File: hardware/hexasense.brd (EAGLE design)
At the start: 100 x 62 mm, 41 parts

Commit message: added GND around PWM lines leading to LEDs
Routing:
- net N$4: track 91.8 -> 100.8 mm
- net N$19: track 75.8 -> 83.9 mm, vias 1 -> 0
- net N$7: track 78.1 -> 84.7 mm
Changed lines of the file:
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@@
 <via x="89.46" y="24.19" extent="1-16" drill="0.3"/>
 <via x="70.96" y="2.73" extent="1-16" drill="0.3"/>
+<polygon width="0.254" layer="1" isolate="0.254" orphans="yes">
+<vertex x="65.77" y="31.02"/>
+<vertex x="65.77" y="47.78"/>
+<vertex x="57.36" y="56.19"/>
+<vertex x="17.49" y="56.19"/>
+<vertex x="17.49" y="52.95"/>
+<vertex x="17.49" y="51.49"/>
+<vertex x="40.61" y="51.49"/>
+<vertex x="56.26" y="51.49"/>
+<vertex x="61.43" y="46.32"/>
+<vertex x="61.43" y="31.02"/>
+</polygon>
 <wire x1="41.11" y1="43.83" x2="41.085" y2="46.89" width="0" layer="19" extent="16-16"/>
 </signal>
@@
 <contactref element="LED4" pad="K"/>
 <contactref element="U$3" pad="P$7"/>
-<wire x1="14.1" y1="60.27" x2="19.2" y2="60.27" width="0.254" layer="16"/>
-<wire x1="19.2" y1="60.27" x2="20.53" y2="58.94" width="0.254" layer="16"/>
-<wire x1="20.53" y1="58.94" x2="36.98" y2="58.94" width="0.254" layer="16"/>
-<wire x1="36.98" y1="58.94" x2="56.39" y2="39.53" width="0.254" layer="16"/>
-<wire x1="56.39" y1="39.53" x2="63.72" y2="39.53" width="0.254" layer="16"/>
-<via x="63.72" y="39.53" extent="1-16" drill="0.3"/>
-<wire x1="63.72" y1="39.53" x2="63.72" y2="17.02" width="0.254" layer="1"/>
-<wire x1="63.72" y1="17.02" x2="64.67" y2="16.07" width="0.254" layer="1"/>
+<wire x1="63.66" y1="17.33" x2="64.67" y2="16.07" width="0.254" layer="1"/>
 <wire x1="64.67" y1="16.07" x2="64.67" y2="15.19" width="0.254" layer="1"/>
 <wire x1="64.67" y1="15.19" x2="63.03" y2="13.55" width="0.254" layer="1"/>
@@
 <wire x1="65.85" y1="11.63" x2="65.855" y2="11.635" width="0.254" layer="1"/>
 <wire x1="65.855" y1="11.635" x2="68.8" y2="11.635" width="0.254" layer="1"/>
+<wire x1="14.1" y1="60.27" x2="17.69" y2="56.68" width="0.254" layer="16"/>
+<wire x1="17.69" y1="56.68" x2="17.69" y2="52.09" width="0.254" layer="16"/>
+<wire x1="17.69" y1="52.09" x2="18.35" y2="51.43" width="0.254" layer="16"/>
+<via x="23.23" y="53.9" extent="1-16" drill="0.3"/>
+<wire x1="23.23" y1="53.9" x2="56.74" y2="53.91" width="0.254" layer="1"/>
+<wire x1="56.74" y1="53.91" x2="63.66" y2="46.99" width="0.254" layer="1"/>
+<wire x1="63.66" y1="46.99" x2="63.66" y2="17.33" width="0.254" layer="1"/>
+<wire x1="18.35" y1="51.43" x2="20.76" y2="51.43" width="0.254" layer="16"/>
+<wire x1="20.76" y1="51.43" x2="23.23" y2="53.9" width="0.254" layer="16"/>
 </signal>
 <signal name="N$5">
@@
 <contactref element="LED7" pad="K"/>
 <contactref element="U$3" pad="P$10"/>
-<wire x1="18.87" y1="53" x2="42.03" y2="53" width="0.254" layer="16"/>
-<wire x1="42.03" y1="53" x2="56.16" y2="38.87" width="0.254" layer="16"/>
-<wire x1="56.16" y1="38.87" x2="64.97" y2="38.87" width="0.254" layer="16"/>
-<via x="64.97" y="38.87" extent="1-16" drill="0.3"/>
-<wire x1="64.97" y1="38.87" x2="64.97" y2="17.38" width="0.254" layer="1"/>
-<wire x1="64.97" y1="17.38" x2="66.91" y2="15.44" width="0.254" layer="1"/>
+<wire x1="64.75" y1="18.43" x2="64.90110625" y2="18.22083125" width="0.254" layer="1"/>
+<wire x1="64.90110625" y1="18.22083125" x2="66.91" y2="15.44" width="0.254" layer="1"/>
 <wire x1="66.91" y1="15.44" x2="68.795" y2="15.44" width="0.254" layer="1"/>
 <wire x1="68.795" y1="15.44" x2="68.8" y2="15.445" width="0.254" layer="1"/>
+<via x="22.55" y="54.96" extent="1-16" drill="0.3"/>
+<wire x1="22.55" y1="54.96" x2="57.23" y2="54.95" width="0.254" layer="1"/>
+<wire x1="57.23" y1="54.95" x2="64.90110625" y2="47.27889375" width="0.254" layer="1"/>
+<wire x1="64.90110625" y1="47.27889375" x2="64.90110625" y2="18.22083125" width="0.254" layer="1"/>
+<wire x1="18.87" y1="53" x2="20.59" y2="53" width="0.254" layer="16"/>
+<wire x1="20.59" y1="53" x2="22.55" y2="54.96" width="0.254" layer="16"/>
 </signal>
 <signal name="N$8">
@@
 <contactref element="LED10" pad="K"/>
 <contactref element="U$3" pad="P$14"/>
-<via x="62.5" y="40.35" extent="1-16" drill="0.3"/>
-<wire x1="62.5" y1="17.34" x2="61.88" y2="16.72" width="0.254" layer="1"/>
 <wire x1="61.88" y1="16.72" x2="59.605" y2="16.72" width="0.254" layer="1"/>
 <wire x1="59.605" y1="16.72" x2="59.6" y2="16.715" width="0.254" layer="1"/>
-<wire x1="21.1" y1="60.27" x2="42.58" y2="60.27" width="0.254" layer="16"/>
-<wire x1="42.58" y1="60.27" x2="62.5" y2="40.35" width="0.254" layer="16"/>
-<wire x1="62.5" y1="17.34" x2="62.5" y2="40.35" width="0.254" layer="1"/>
+<wire x1="21.1" y1="60.27" x2="19.53" y2="58.7" width="0.254" layer="1"/>
+<wire x1="19.53" y1="58.7" x2="19.53" y2="56.19" width="0.254" layer="1"/>
+<wire x1="62.39" y1="46.62" x2="56.37" y2="52.64" width="0.254" layer="1"/>
+<wire x1="56.37" y1="52.64" x2="23.08" y2="52.64" width="0.254" layer="1"/>
+<wire x1="23.08" y1="52.64" x2="19.53" y2="56.19" width="0.254" layer="1"/>
+<wire x1="62.39" y1="46.62" x2="62.39" y2="17.23" width="0.254" layer="1"/>
+<wire x1="62.39" y1="17.23" x2="61.88" y2="16.72" width="0.254" layer="1"/>
 </signal>
 <signal name="N$20">

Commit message: changed something
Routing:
- net GND: track 57.2 -> 70.8 mm, vias 7 -> 8
- net DATA: track 68.2 -> 67.7 mm
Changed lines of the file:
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@@
 <via x="70.96" y="2.73" extent="1-16" drill="0.3"/>
 <polygon width="0.254" layer="1" isolate="0.254" orphans="yes">
-<vertex x="65.77" y="31.02"/>
+<vertex x="65.77" y="32.5"/>
 <vertex x="65.77" y="47.78"/>
 <vertex x="57.36" y="56.19"/>
 <vertex x="17.49" y="56.19"/>
-<vertex x="17.49" y="52.95"/>
 <vertex x="17.49" y="51.49"/>
-<vertex x="40.61" y="51.49"/>
 <vertex x="56.26" y="51.49"/>
 <vertex x="61.43" y="46.32"/>
-<vertex x="61.43" y="31.02"/>
+<vertex x="61.43" y="32.5"/>
 </polygon>
-<wire x1="41.11" y1="43.83" x2="41.085" y2="46.89" width="0" layer="19" extent="16-16"/>
+<wire x1="61.75" y1="31.1" x2="61.75" y2="32.97" width="0.16" layer="1"/>
+<wire x1="63.03" y1="30.88" x2="63.03" y2="32.95" width="0.16" layer="1"/>
+<wire x1="65.43" y1="30.98" x2="65.43" y2="33.01" width="0.16" layer="1"/>
+<wire x1="64.31" y1="32.51" x2="64.31" y2="30.87" width="0.16" layer="1"/>
+<wire x1="41.085" y1="46.89" x2="43.14" y2="46.89" width="0.254" layer="16"/>
+<via x="43.14" y="46.89" extent="1-16" drill="0.3"/>
+<wire x1="43.14" y1="46.89" x2="43.14" y2="45.86" width="0.254" layer="1"/>
+<wire x1="43.14" y1="45.86" x2="41.11" y2="43.83" width="0.254" layer="1"/>
+<wire x1="64.31" y1="30.87" x2="65.43" y2="30.98" width="0" layer="19" extent="1-1"/>
+<wire x1="61.75" y1="31.1" x2="63.03" y2="30.88" width="0" layer="19" extent="1-1"/>
 </signal>
 <signal name="+3V3">
@@
 <wire x1="33.5" y1="18.89" x2="37.57" y2="18.89" width="0.254" layer="1"/>
 <wire x1="37.57" y1="18.89" x2="37.97" y2="18.49" width="0.254" layer="1"/>
-<wire x1="24.96" y1="43.68" x2="32.67" y2="43.68" width="0.254" layer="1"/>
-<wire x1="32.67" y1="43.68" x2="32.83" y2="43.68" width="0.254" layer="1"/>
+<wire x1="24.96" y1="43.68" x2="32.74" y2="43.68" width="0.254" layer="1"/>
+<wire x1="32.74" y1="43.68" x2="32.83" y2="43.68" width="0.254" layer="1"/>
 <wire x1="32.83" y1="43.68" x2="37.33" y2="48.18" width="0.254" layer="1"/>
 <via x="37.33" y="48.18" extent="1-16" drill="0.3"/>
 <wire x1="37.33" y1="48.18" x2="41.095" y2="48.18" width="0.254" layer="16"/>
 <wire x1="41.095" y1="48.18" x2="41.1" y2="48.175" width="0.254" layer="16"/>
-<wire x1="41.11" y1="36.21" x2="40.14" y2="36.21" width="0.254" layer="1"/>
-<wire x1="40.14" y1="36.21" x2="32.67" y2="43.68" width="0.254" layer="1"/>
 <wire x1="59.6" y1="4.015" x2="51.345" y2="4.015" width="0.254" layer="1"/>
 <wire x1="51.345" y1="4.015" x2="48.97" y2="1.64" width="0.254" layer="1"/>
@@
 <wire x1="93.68" y1="46.38" x2="94.51" y2="47.21" width="0.254" layer="1"/>
 <wire x1="94.51" y1="47.21" x2="94.51" y2="48.99" width="0.254" layer="1"/>
+<wire x1="41.11" y1="36.21" x2="33.64" y2="43.68" width="0.254" layer="1"/>
+<wire x1="33.64" y1="43.68" x2="32.83" y2="43.68" width="0.254" layer="1"/>
 </signal>
 <signal name="TEMP_1">
@@
 <contactref element="U$6" pad="DATA"/>
 <wire x1="40.51" y1="18.49" x2="40.51" y2="33.2" width="0.254" layer="1"/>
-<wire x1="40.51" y1="33.2" x2="42.97" y2="35.66" width="0.254" layer="1"/>
-<wire x1="42.97" y1="35.66" x2="42.97" y2="36.89" width="0.254" layer="1"/>
-<wire x1="42.97" y1="36.89" x2="41.11" y2="38.75" width="0.254" layer="1"/>
 <wire x1="24.96" y1="46.22" x2="21.55" y2="46.22" width="0.254" layer="1"/>
 <wire x1="3.2" y1="46.73" x2="5.2" y2="44.73" width="0.254" layer="1"/>
@@
 <wire x1="35.47" y1="44.92" x2="26.26" y2="44.92" width="0.254" layer="16"/>
 <wire x1="26.26" y1="44.92" x2="24.96" y2="46.22" width="0.254" layer="16"/>
+<wire x1="41.11" y1="38.75" x2="42.33" y2="37.53" width="0.254" layer="1"/>
+<wire x1="42.33" y1="37.53" x2="42.33" y2="34.99" width="0.254" layer="1"/>
+<wire x1="42.33" y1="34.99" x2="40.54" y2="33.2" width="0.254" layer="1"/>
+<wire x1="40.54" y1="33.2" x2="40.51" y2="33.2" width="0.254" layer="1"/>
 </signal>
 <signal name="SDA">
@@
 <wire x1="68.13" y1="37.13" x2="57.28" y2="37.13" width="0.254" layer="16"/>
 <wire x1="57.28" y1="37.13" x2="57.03" y2="37.14" width="0.254" layer="16"/>
-<wire x1="57.03" y1="37.14" x2="60.48" y2="34.78" width="0.254" layer="1"/>
-<wire x1="60.48" y1="34.78" x2="60.48" y2="22.53" width="0.254" layer="1"/>
 <wire x1="60.48" y1="22.53" x2="58.38" y2="20.43" width="0.254" layer="1"/>
 <wire x1="71.04" y1="34.22" x2="68.13" y2="37.13" width="0.254" layer="16"/>
 <wire x1="44.485" y1="49.475" x2="56.82" y2="37.14" width="0.254" layer="16"/>
 <wire x1="56.82" y1="37.14" x2="57.03" y2="37.14" width="0.254" layer="16"/>
+<wire x1="57.03" y1="37.14" x2="60.48" y2="33.69" width="0.254" layer="1"/>
+<wire x1="60.48" y1="33.69" x2="60.48" y2="22.53" width="0.254" layer="1"/>
 </signal>
 <signal name="BTN">

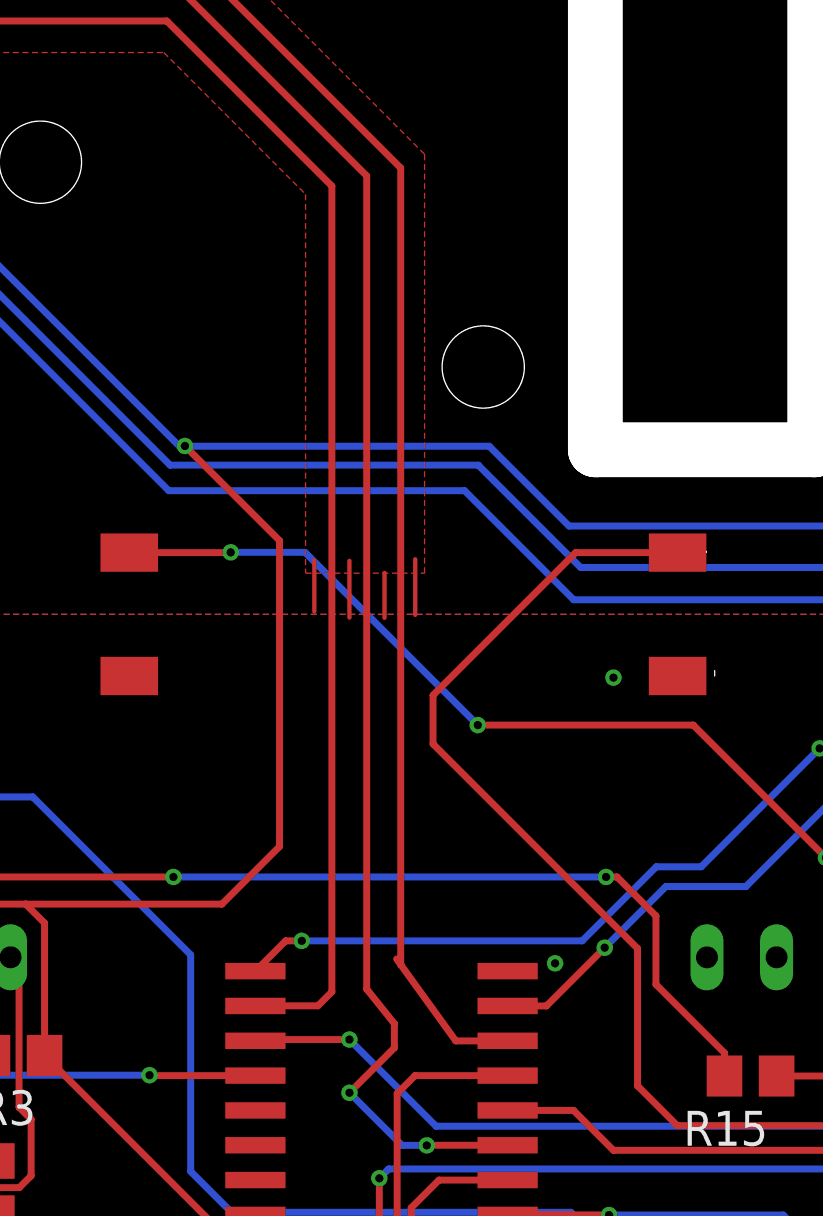
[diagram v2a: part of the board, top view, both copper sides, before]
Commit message: bend wires in 45 deg angle
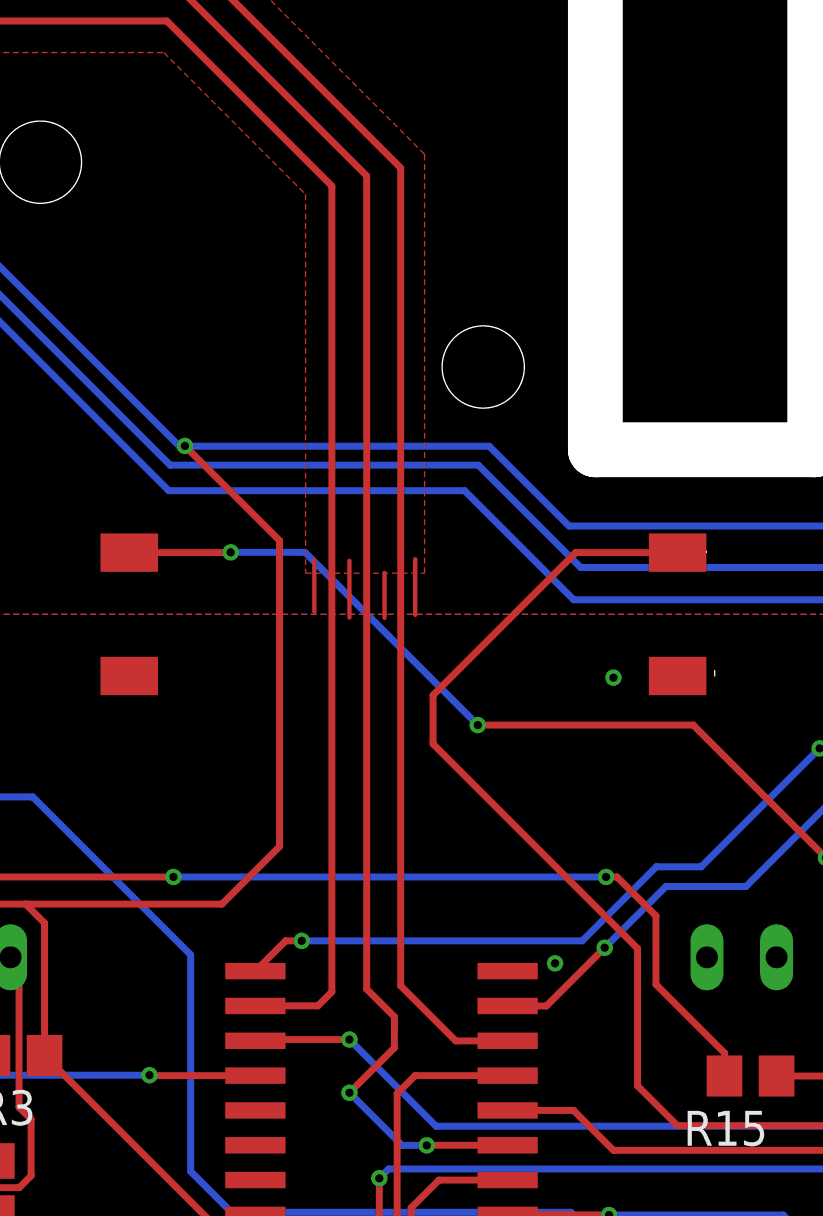
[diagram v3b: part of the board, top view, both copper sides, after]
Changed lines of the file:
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@@
 <wire x1="43.14" y1="45.86" x2="41.11" y2="43.83" width="0.254" layer="1"/>
 <wire x1="64.31" y1="30.87" x2="65.43" y2="30.98" width="0" layer="19" extent="1-1"/>
+<wire x1="63.03" y1="30.88" x2="64.31" y2="30.87" width="0" layer="19" extent="1-1"/>
 <wire x1="61.75" y1="31.1" x2="63.03" y2="30.88" width="0" layer="19" extent="1-1"/>
 </signal>
@@
 <contactref element="LED4" pad="K"/>
 <contactref element="U$3" pad="P$7"/>
-<wire x1="63.66" y1="17.33" x2="64.67" y2="16.07" width="0.254" layer="1"/>
-<wire x1="64.67" y1="16.07" x2="64.67" y2="15.19" width="0.254" layer="1"/>
+<wire x1="64.67" y1="16.07" x2="64.67" y2="15.9" width="0.254" layer="1"/>
+<wire x1="64.67" y1="15.9" x2="64.67" y2="15.19" width="0.254" layer="1"/>
 <wire x1="64.67" y1="15.19" x2="63.03" y2="13.55" width="0.254" layer="1"/>
 <via x="63.03" y="13.55" extent="1-16" drill="0.3"/>
@@
 <wire x1="18.35" y1="51.43" x2="20.76" y2="51.43" width="0.254" layer="16"/>
 <wire x1="20.76" y1="51.43" x2="23.23" y2="53.9" width="0.254" layer="16"/>
+<wire x1="63.66" y1="17.33" x2="64.67" y2="16.32" width="0.254" layer="1"/>
+<wire x1="64.67" y1="16.32" x2="64.67" y2="16.07" width="0.254" layer="1"/>
 </signal>
 <signal name="N$5">
@@
 <contactref element="LED7" pad="K"/>
 <contactref element="U$3" pad="P$10"/>
-<wire x1="64.75" y1="18.43" x2="64.90110625" y2="18.22083125" width="0.254" layer="1"/>
-<wire x1="64.90110625" y1="18.22083125" x2="66.91" y2="15.44" width="0.254" layer="1"/>
 <wire x1="66.91" y1="15.44" x2="68.795" y2="15.44" width="0.254" layer="1"/>
 <wire x1="68.795" y1="15.44" x2="68.8" y2="15.445" width="0.254" layer="1"/>
@@
 <wire x1="22.55" y1="54.96" x2="57.23" y2="54.95" width="0.254" layer="1"/>
 <wire x1="57.23" y1="54.95" x2="64.90110625" y2="47.27889375" width="0.254" layer="1"/>
-<wire x1="64.90110625" y1="47.27889375" x2="64.90110625" y2="18.22083125" width="0.254" layer="1"/>
+<wire x1="64.90110625" y1="47.27889375" x2="64.90110625" y2="17.44889375" width="0.254" layer="1"/>
 <wire x1="18.87" y1="53" x2="20.59" y2="53" width="0.254" layer="16"/>
 <wire x1="20.59" y1="53" x2="22.55" y2="54.96" width="0.254" layer="16"/>
+<wire x1="64.90110625" y1="17.44889375" x2="66.91" y2="15.44" width="0.254" layer="1"/>
 </signal>
 <signal name="N$8">

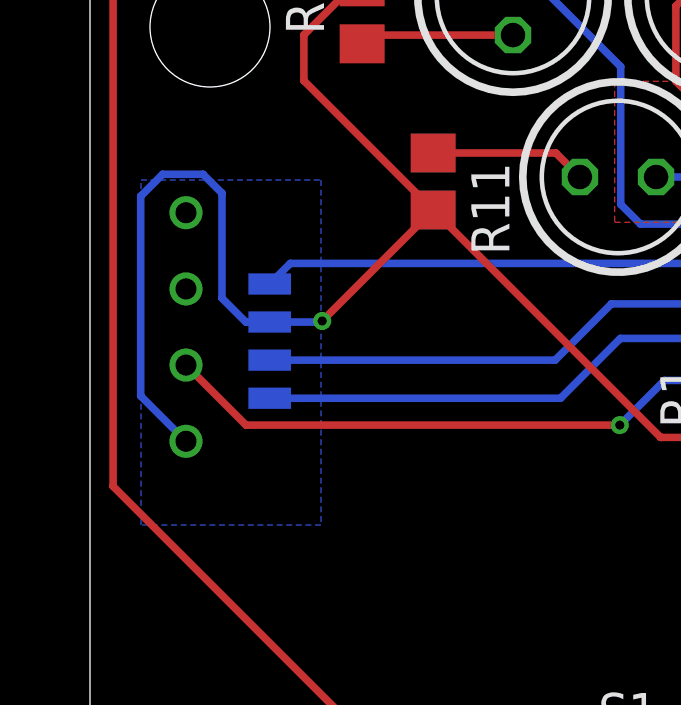
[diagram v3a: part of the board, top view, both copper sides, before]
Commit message: removed unneeded GND polygon
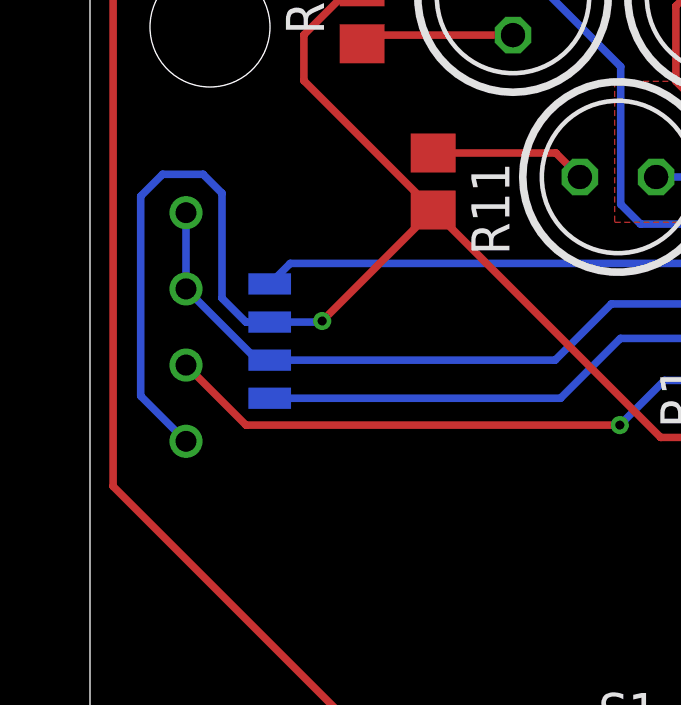
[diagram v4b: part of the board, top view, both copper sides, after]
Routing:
- net GND: track 70.8 -> 77.1 mm
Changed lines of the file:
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@@
 <vertex x="0" y="31"/>
-</polygon>
-<polygon width="0.254" layer="16" spacing="0.254" isolate="0.254" orphans="yes">
-<vertex x="7.7" y="52.9"/>
-<vertex x="7.7" y="41.4"/>
-<vertex x="1.7" y="41.4"/>
-<vertex x="1.7" y="52.9"/>
 </polygon>
 <via x="90.79" y="29.54" extent="1-16" drill="0.3"/>
@@
 <wire x1="63.03" y1="30.88" x2="64.31" y2="30.87" width="0" layer="19" extent="1-1"/>
 <wire x1="61.75" y1="31.1" x2="63.03" y2="30.88" width="0" layer="19" extent="1-1"/>
+<wire x1="3.2" y1="51.81" x2="3.2" y2="49.27" width="0.254" layer="16"/>
+<wire x1="5.99" y1="46.895" x2="5.575" y2="46.895" width="0.254" layer="16"/>
+<wire x1="5.575" y1="46.895" x2="3.2" y2="49.27" width="0.254" layer="16"/>
 </signal>
 <signal name="+3V3">
